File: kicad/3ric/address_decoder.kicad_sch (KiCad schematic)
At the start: 39 parts

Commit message: picking up steam on the layout - lots of progress
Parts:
- added U1: 74LS08, symbol 74xx:74LS08
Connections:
- net ~{DEVICE}: now also U1.4; no longer U?.10, U?.13
- new net DISKSS: U1.5
- new net ~{DEVICE2}: U1.6, U?.10, U?.13
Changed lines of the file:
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@@
 	)
 	(junction
-		(at 175.26 97.79)
+		(at 26.67 44.45)
 		(diameter 0)
 		(color 0 0 0 0)
 	)
 	(junction
-		(at 26.67 44.45)
+		(at 163.83 119.38)
 		(diameter 0)
 		(color 0 0 0 0)
@@
 	)
 	(junction
+		(at 193.04 121.92)
+		(diameter 0)
+		(color 0 0 0 0)
+	)
+	(junction
 		(at 66.04 110.49)
 		(diameter 0)
@@
 	(wire
 		(pts
+			(xy 193.04 107.95) (xy 175.26 107.95)
+		)
+		(stroke
+			(width 0)
+			(type default)
+		)
+	)
+	(wire
+		(pts
 			(xy 46.99 167.64) (xy 50.8 167.64)
 		)
@@
 	(wire
 		(pts
-			(xy 175.26 97.79) (xy 175.26 83.82)
+			(xy 175.26 83.82) (xy 175.26 107.95)
 		)
 		(stroke
@@
 	(wire
 		(pts
+			(xy 193.04 121.92) (xy 193.04 107.95)
+		)
+		(stroke
+			(width 0)
+			(type default)
+		)
+	)
+	(wire
+		(pts
 			(xy 26.67 27.94) (xy 55.88 27.94)
 		)
@@
 	(wire
 		(pts
+			(xy 163.83 119.38) (xy 175.26 119.38)
+		)
+		(stroke
+			(width 0)
+			(type default)
+		)
+	)
+	(wire
+		(pts
 			(xy 46.99 71.12) (xy 50.8 71.12)
 		)
@@
 	(wire
 		(pts
-			(xy 161.29 119.38) (xy 175.26 119.38)
+			(xy 161.29 119.38) (xy 163.83 119.38)
 		)
 		(stroke
@@
 	(wire
 		(pts
+			(xy 163.83 113.03) (xy 163.83 119.38)
+		)
+		(stroke
+			(width 0)
+			(type default)
+		)
+	)
+	(wire
+		(pts
 			(xy 90.17 33.02) (xy 93.98 33.02)
 		)
@@
 	(wire
 		(pts
-			(xy 46.99 71.12) (xy 46.99 76.2)
+			(xy 193.04 121.92) (xy 198.12 121.92)
 		)
 		(stroke
@@
 	(wire
 		(pts
-			(xy 175.26 97.79) (xy 180.34 97.79)
+			(xy 46.99 71.12) (xy 46.99 76.2)
 		)
 		(stroke
@@
 	(wire
 		(pts
+			(xy 193.04 121.92) (xy 190.5 121.92)
+		)
+		(stroke
+			(width 0)
+			(type default)
+		)
+	)
+	(wire
+		(pts
 			(xy 252.73 129.54) (xy 255.27 129.54)
 		)
@@
 	(wire
 		(pts
+			(xy 193.04 123.19) (xy 193.04 121.92)
+		)
+		(stroke
+			(width 0)
+			(type default)
+		)
+	)
+	(wire
+		(pts
 			(xy 67.31 68.58) (xy 67.31 77.47)
 		)
@@
 	(wire
 		(pts
-			(xy 175.26 119.38) (xy 175.26 97.79)
-		)
-		(stroke
-			(width 0)
-			(type default)
-		)
-	)
-	(wire
-		(pts
 			(xy 240.03 83.82) (xy 240.03 92.71)
 		)
@@
 		)
 	)
-	(global_label "~{DEVICE}"
-		(shape input)
-		(at 180.34 97.79 0)
-		(fields_autoplaced yes)
-		(effects
-			(font
-				(size 1.27 1.27)
-			)
-			(justify left)
-		)
-		(property "Intersheetrefs" "${INTERSHEET_REFS}"
-			(at 189.2845 97.7106 0)
-			(effects
-				(font
-					(size 1.27 1.27)
-				)
-				(justify left)
-				(hide yes)
-			)
-		)
-	)
 	(global_label "CA14"
 		(shape input)
@@
 		)
 	)
-	(global_label "~{DEVICE}"
-		(shape input)
-		(at 242.57 58.42 180)
-		(fields_autoplaced yes)
-		(effects
-			(font
-				(size 1.27 1.27)
-			)
-			(justify right)
-		)
-		(property "Intersheetrefs" "${INTERSHEET_REFS}"
-			(at 233.6255 58.3406 0)
-			(effects
-				(font
-					(size 1.27 1.27)
-				)
-				(justify right)
-				(hide yes)
-			)
-		)
-	)
 	(global_label "CA8"
 		(shape input)
@@
 		)
 	)
+	(global_label "~{DEVICE2}"
+		(shape input)
+		(at 198.12 121.92 0)
+		(fields_autoplaced yes)
+		(effects
+			(font
+				(size 1.27 1.27)
+			)
+			(justify left)
+		)
+		(property "Intersheetrefs" "${INTERSHEET_REFS}"
+			(at 208.8461 121.92 0)
+			(effects
+				(font
+					(size 1.27 1.27)
+				)
+				(justify left)
+				(hide yes)
+			)
+		)
+	)
 	(global_label "CA14"
 		(shape input)
@@
 		)
 	)
+	(global_label "~{DEVICE2}"
+		(shape input)
+		(at 242.57 58.42 180)
+		(fields_autoplaced yes)
+		(effects
+			(font
+				(size 1.27 1.27)
+			)
+			(justify right)
+		)
+		(property "Intersheetrefs" "${INTERSHEET_REFS}"
+			(at 231.8439 58.42 0)
+			(effects
+				(font
+					(size 1.27 1.27)
+				)
+				(justify right)
+				(hide yes)
+			)
+		)
+	)
 	(global_label "DXXX"
 		(shape input)
@@
 		)
 	)
+	(global_label "~{DEVICE}"
+		(shape input)
+		(at 163.83 113.03 0)
+		(fields_autoplaced yes)
+		(effects
+			(font
+				(size 1.27 1.27)
+			)
+			(justify left)
+		)
+		(property "Intersheetrefs" "${INTERSHEET_REFS}"
+			(at 172.7745 112.9506 0)
+			(effects
+				(font
+					(size 1.27 1.27)
+				)
+				(justify left)
+				(hide yes)
+			)
+		)
+	)
 	(global_label "CA14"
 		(shape input)
@@
 		)
 	)
+	(global_label "DISKSS"
+		(shape input)
+		(at 175.26 124.46 180)
+		(fields_autoplaced yes)
+		(effects
+			(font
+				(size 1.27 1.27)
+			)
+			(justify right)
+		)
+		(property "Intersheetrefs" "${INTERSHEET_REFS}"
+			(at 165.5015 124.46 0)
+			(effects
+				(font
+					(size 1.27 1.27)
+				)
+				(justify right)
+				(hide yes)
+			)
+		)
+	)
 	(global_label "!VIDENABLE"
 		(shape input)
@@
 				)
 			)
+		)
+	)
+	(symbol
+		(lib_id "74xx:74LS08")
+		(at 182.88 121.92 0)
+		(unit 2)
+		(exclude_from_sim no)
+		(in_bom yes)
+		(on_board yes)
+		(dnp no)
+		(fields_autoplaced yes)
+		(property "Reference" "U1"
+			(at 182.88 114.4102 0)
+			(effects
+				(font
+					(size 1.27 1.27)
+				)
+			)
+		)
+		(property "Value" "74LS08"
+			(at 182.88 116.9471 0)
+			(effects
+				(font
+					(size 1.27 1.27)
+				)
+			)
+		)
+		(property "Footprint" ""
+			(at 182.88 121.92 0)
+			(effects
+				(font
+					(size 1.27 1.27)
+				)
+				(hide yes)
+			)
+		)
+		(property "Datasheet" "http://www.ti.com/lit/gpn/sn74LS08"
+			(at 182.88 121.92 0)
+			(effects
+				(font
+					(size 1.27 1.27)
+				)
+				(hide yes)
+			)
+		)
+		(property "Description" ""
+			(at 182.88 121.92 0)
+			(effects
+				(font
+					(size 1.27 1.27)
+				)
+				(hide yes)
+			)
+		)
+		(pin "1"
+		)
+		(pin "2"
+		)
+		(pin "3"
+		)
+		(pin "4"
+		)
+		(pin "5"
+		)
+		(pin "6"
+		)
+		(pin "10"
+		)
+		(pin "8"
+		)
+		(pin "9"
+		)
+		(pin "11"
+		)
+		(pin "12"
+		)
+		(pin "13"
+		)
+		(pin "14"
+		)
+		(pin "7"
+		)
+		(instances
+			(project "3ric"
+				(path "/e63e39d7-6ac0-4ffd-8aa3-1841a4541b55/b718fcb1-8742-4b46-85e8-c35e05bc00ea"
+					(reference "U1")
+					(unit 2)
+				)
+			)

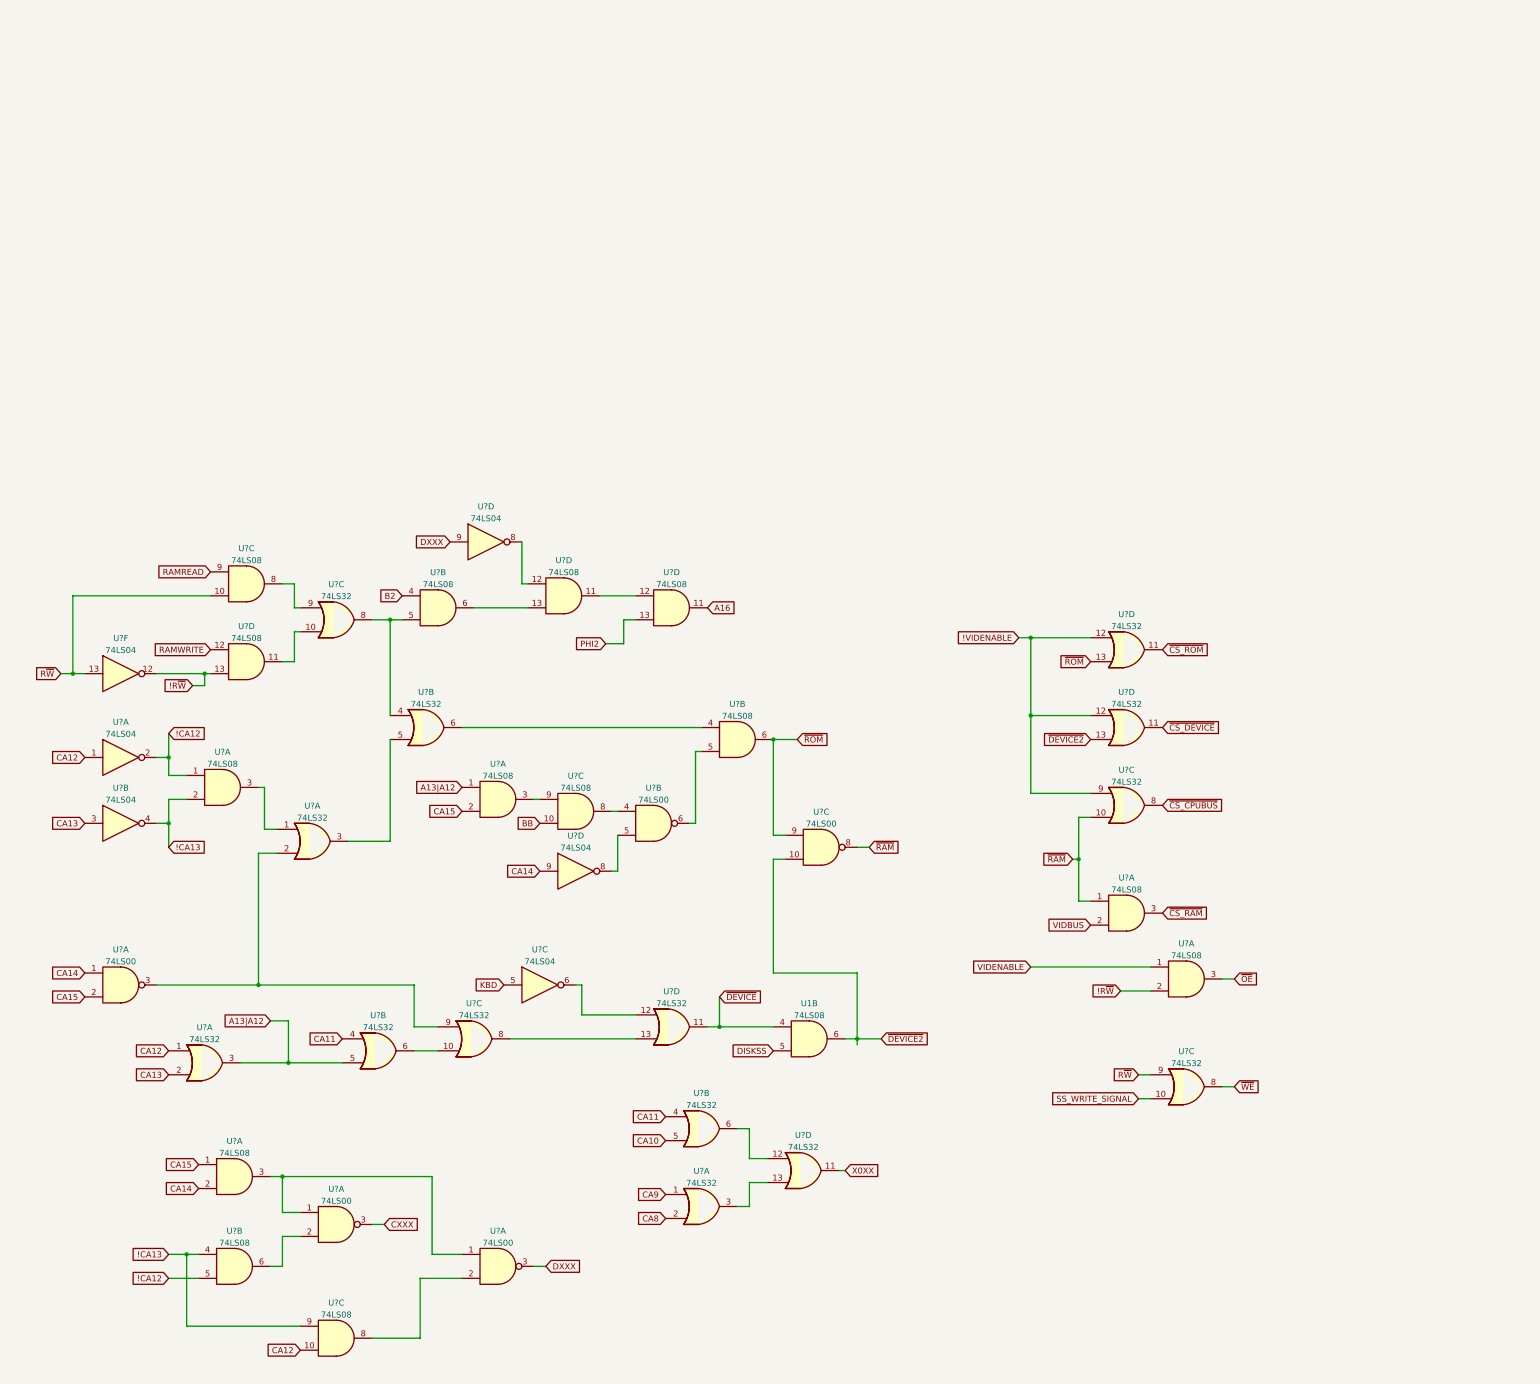
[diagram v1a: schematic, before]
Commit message: update units for soft switch logic to match breadboard
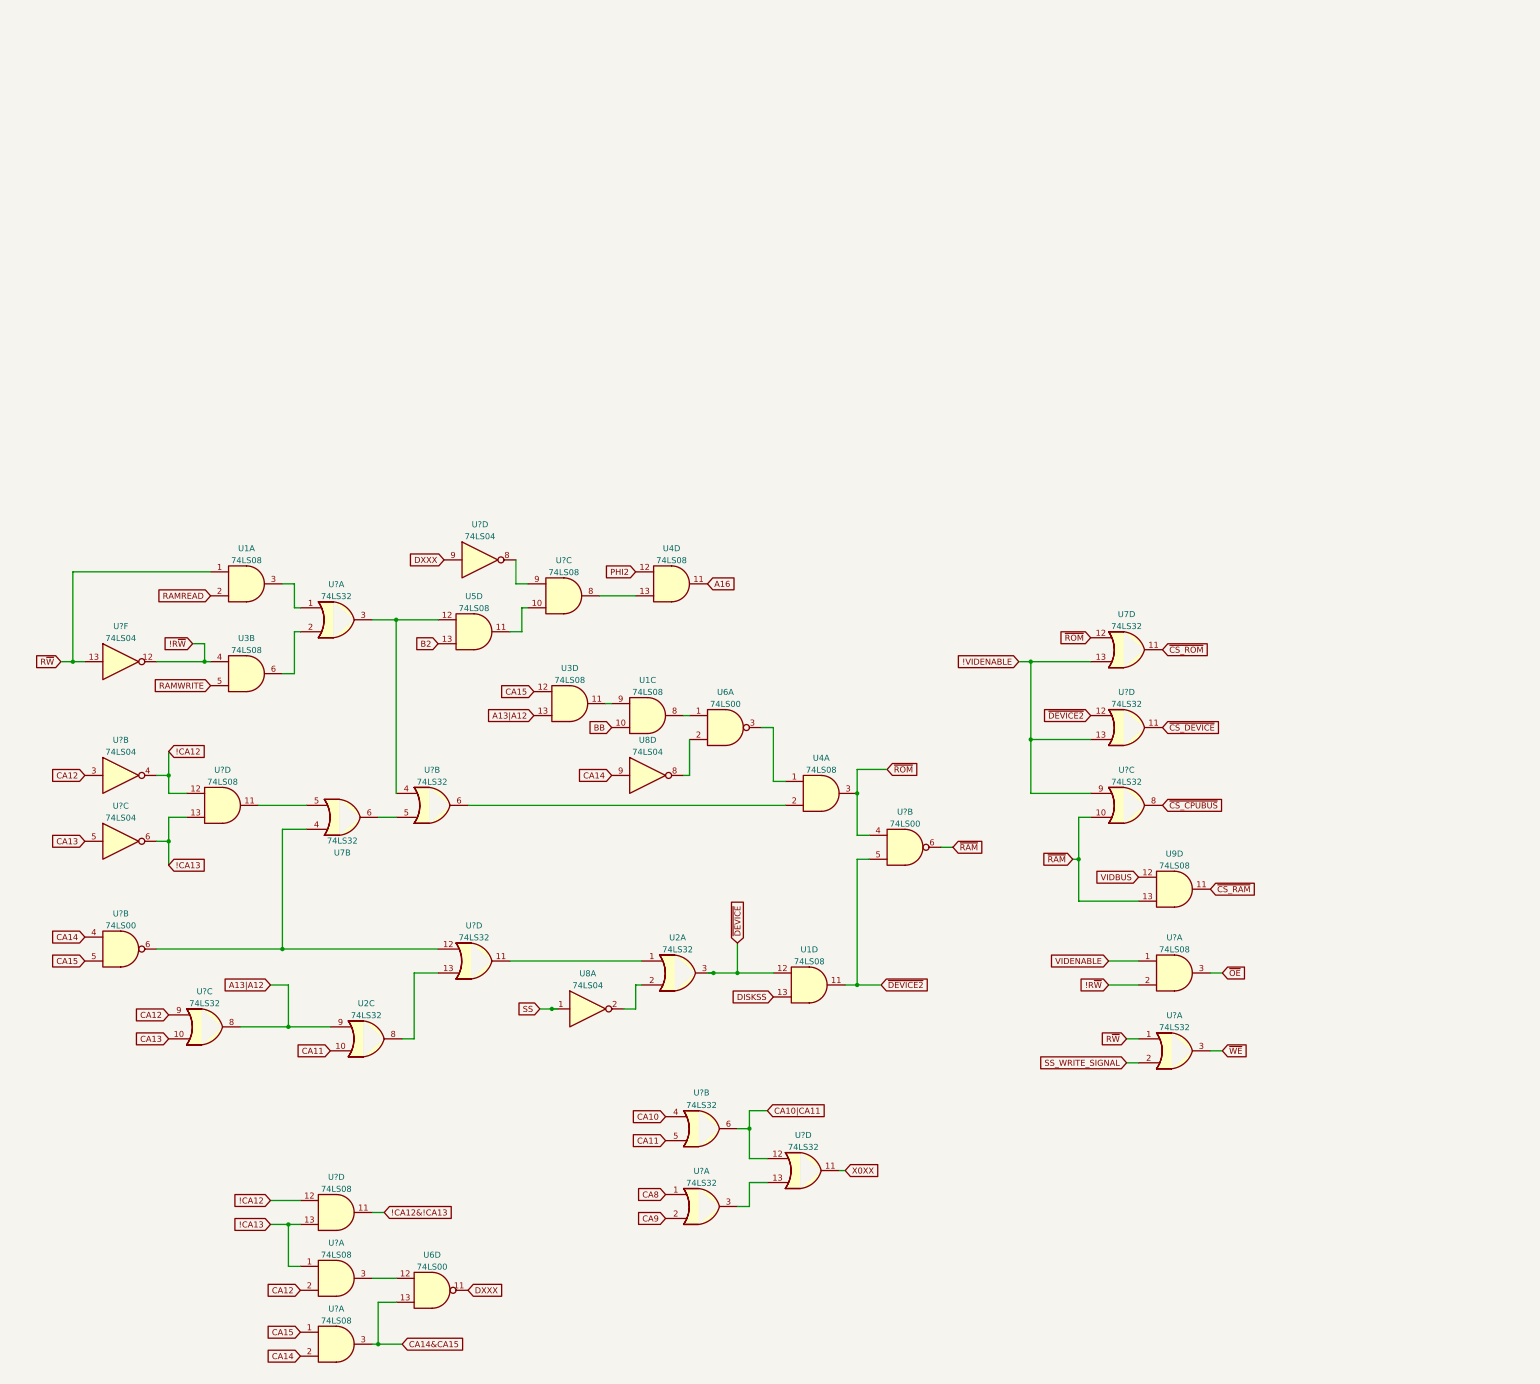
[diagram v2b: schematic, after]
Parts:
- removed U? (x2): 74LS04, symbol 74xx:74LS04
- removed U? (x8): 74LS08, symbol 74xx:74LS08
- removed U? (x4): 74LS32, symbol 74xx:74LS32
- removed U? (x3): 74LS00, symbol 74xx:74LS00
- added unit 3 of U1
- added unit 1 of U1
- added U2, U7: 74LS32, symbol 74xx:74LS32
- added U3, U4, U5, U9: 74LS08, symbol 74xx:74LS08
- added U6: 74LS00, symbol 74xx:74LS00
- added U8: 74LS04, symbol 74xx:74LS04
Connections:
- net !CA12: now also U?.12, U?.12, U?.4; no longer U?.1, U?.2, U?.5
- net !CA13: now also U?.1, U?.13, U?.13, U?.6; no longer U?.2, U?.4, U?.4, U?.9
- net !R~{W}: now also U3.4
- net !VIDENABLE: now also U?.13, U7.13; no longer U?.12
- net A13|A12: now also U?.8, U2.9, U3.13; no longer U?.3
- net A16: now also U4.11
- net B2: now also U5.13
- net BB: now also U1.10
- net CA10: now also U?.4; no longer U?.5
- net CA11: now also U?.5, U2.10; no longer U?.4
- net CA12: now also U?.2, U?.3, U?.9; no longer U?.1, U?.1, U?.10
- net CA13: now also U?.10, U?.5; no longer U?.2, U?.3
- net CA14: now also U?.4, U8.9; no longer U?.1
- net CA15: now also U?.5, U3.12; no longer U?.2
- net CA8: now also U?.1; no longer U?.2
- net CA9: now also U?.2; no longer U?.1
- net DISKSS: now also U1.13; no longer U1.5
- net DXXX: now also U6.11
- net PHI2: now also U4.12
- net RAMREAD: now also U1.2
- net RAMWRITE: now also U3.5
- net R~{W}: now also U?.1, U1.1; no longer U?.9
- net SS_WRITE_SIGNAL: now also U?.2; no longer U?.10
- net VIDBUS: now also U9.12
- net ~{CS_RAM}: now also U9.11
- net ~{CS_ROM}: now also U7.11
- net ~{DEVICE2}: now also U1.11, U?.12, U?.5; no longer U1.6, U?.10, U?.13
- net ~{DEVICE}: now also U1.12, U2.3; no longer U1.4
- net ~{RAM}: now also U?.6, U9.13; no longer U?.8
- net ~{ROM}: now also U?.4, U4.3, U7.12; no longer U?.9
- net ~{WE}: now also U?.3; no longer U?.8
- net CA14&CA15: now reaches U?.3
- net CA14&CA15: now also U6.13
- net at U?.8: now also U?.9; no longer U?.12
- net at U?.4: now also U?.3, U5.12; no longer U?.8
- net at U?.5: now also U7.6
- net at U?.6: now also U4.2
- net CA10|CA11: now reaches U?.12, U?.6
- new net: U3.6, U?.2
- new net: U5.11, U?.10
- new net: U1.8, U6.1
- new net: U6.2, U8.8
- new net: U4.1, U6.3
- new net: U2.1, U?.11
- new net: U2.2, U8.2
- new net: U1.9, U3.11
- new net: U4.13, U?.8
- new net: U2.8, U?.13
- new net: U1.3, U?.1
- new net: U6.12, U?.3
- new net: U7.5, U?.11
- new net: U7.4, U?.12, U?.6
- new net !CA12&!CA13: U?.11
- new net SS: U8.1
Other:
- moved on the sheet: U1D, U?A, U?B, U?C, U?D, U?F

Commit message: update schematic based on breadboard
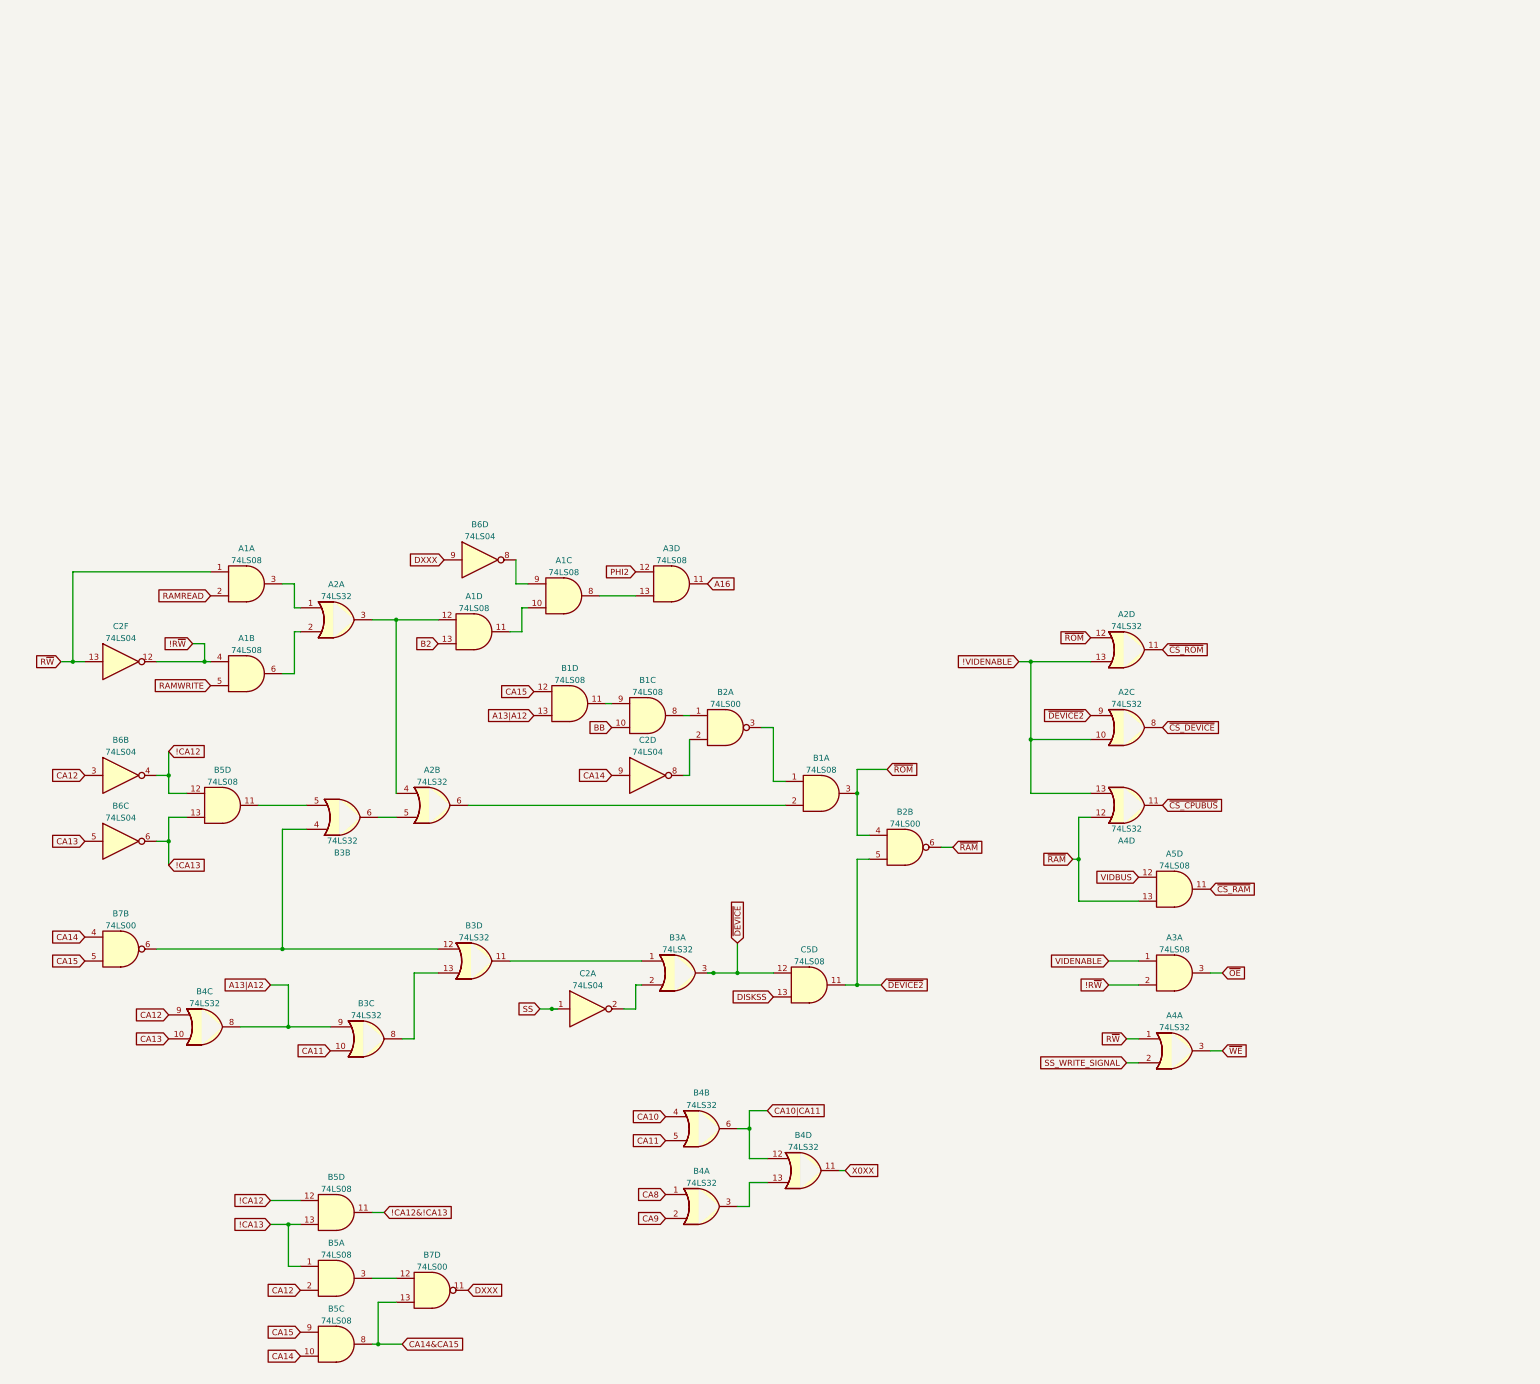
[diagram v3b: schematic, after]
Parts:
- gave numbers to parts that had none: 11
- renumbered U3 to A1, U5 to A1, U1 to A1, U7 to A2, U4 to A3, U9 to A5, U4 to B1, U1 to B1, U3 to B1, U6 to B2, U2 to B3, U7 to B3, U6 to B7, U8 to C2, U1 to C5
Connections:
- net !VIDENABLE: now also A2.10, A4.13; no longer A2.13, A4.9
- net CA14: now also B5.10; no longer B5.2
- net CA14&CA15: now also B5.8; no longer B5.3
- net CA15: now also B5.9; no longer B5.1
- net ~{CS_CPUBUS}: now also A4.11; no longer A4.8
- net ~{CS_DEVICE}: now also A2.8; no longer A2.11
- net ~{DEVICE2}: now also A2.9; no longer A2.12
- net ~{RAM}: now also A4.12; no longer A4.10
